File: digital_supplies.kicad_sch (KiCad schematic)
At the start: 74 parts, among them Q1 PMOS, Q2 2PNP, U19 74LVC1G06, U4 3V3REG, U5 LDO-ADJ, U6 LDO-ADJ, U7 LDO-ADJ

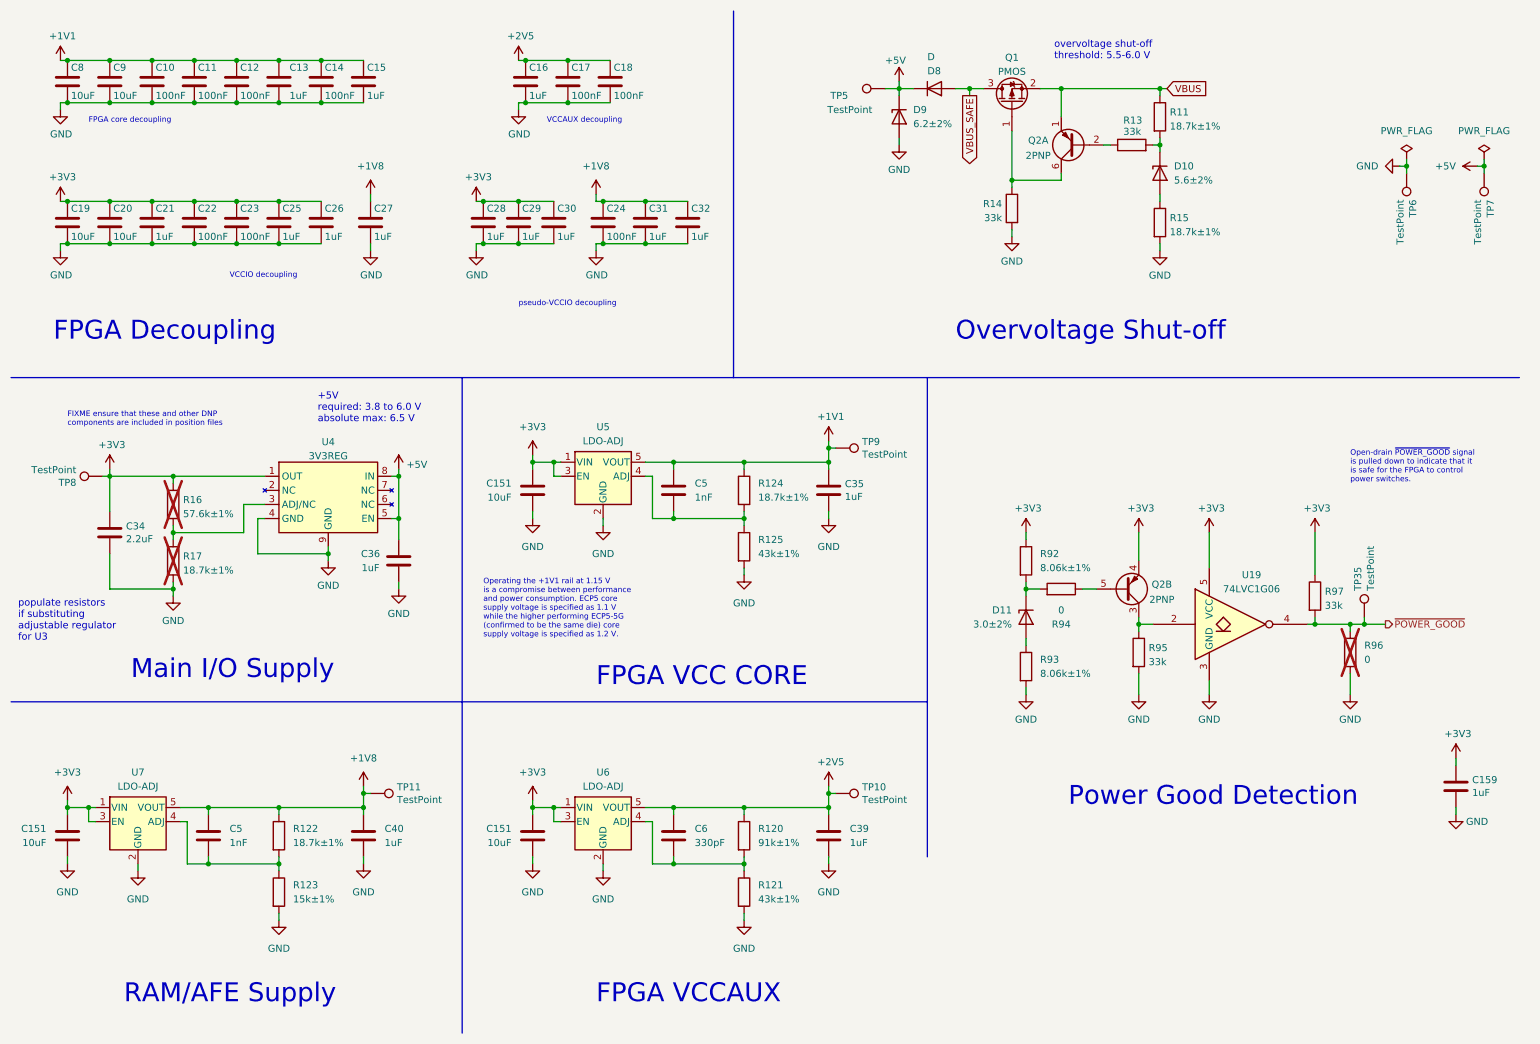
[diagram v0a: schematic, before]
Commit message: add regulator for analog 3.3 V supply
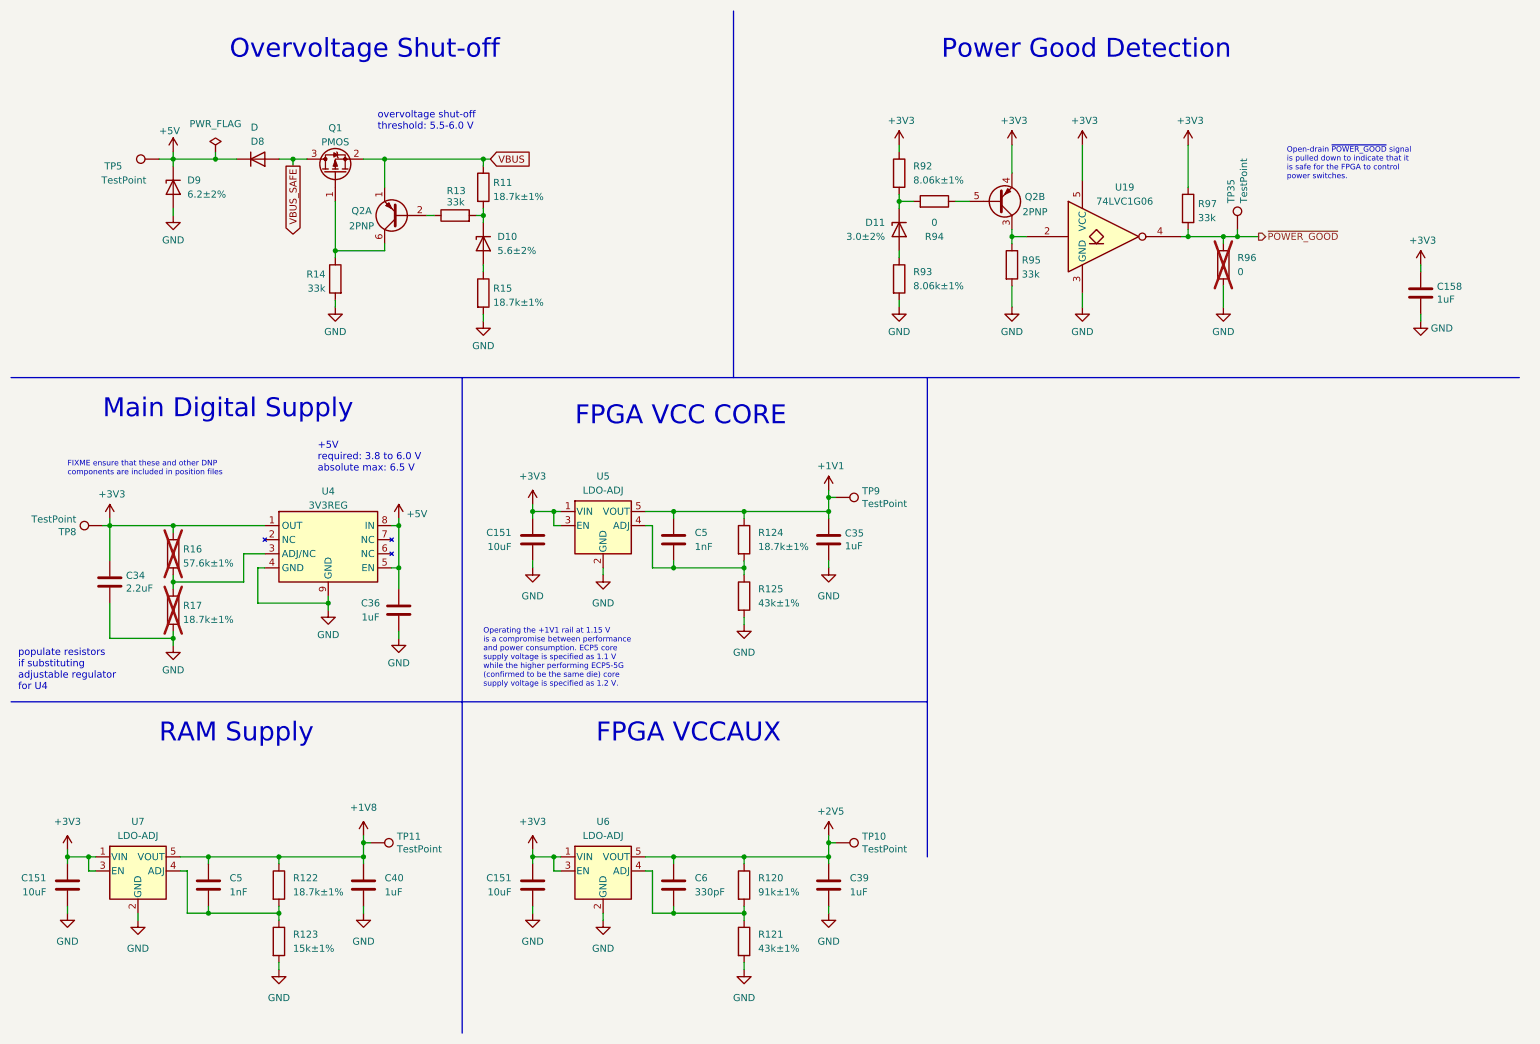
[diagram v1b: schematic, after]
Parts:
- removed C10, C11, C12, C14, C17, C18, C22, C23, C24: 100nF, Capacitor_SMD:C_0402_1005Metric, symbol Device:C
- removed C13, C15, C16, C21, C25, C26, C27, C28, C29, C30, C31, C32: 1uF, Capacitor_SMD:C_0402_1005Metric, symbol Device:C
- removed C19, C20, C8, C9: 10uF, Capacitor_SMD:C_0603_1608Metric, symbol Device:C
- removed TP6, TP7: TestPoint, TestPoint:TestPoint_Pad_D1.0mm, symbol Connector:TestPoint
- renumbered C159 to C158
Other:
- note added: "Main Digital Supply"
- note added: "RAM Supply"
- note added: "populate resistors if substituting adjustable regulator for U4"
- note removed: "FPGA Decoupling"
- note removed: "FPGA core decoupling"
- note removed: "Main I/O Supply"
- note removed: "RAM/AFE Supply"
- note removed: "VCCAUX decoupling"
- note removed: "VCCIO decoupling"
- note removed: "populate resistors if substituting adjustable regulator for U3"
- note removed: "pseudo-VCCIO decoupling"
- moved on the sheet: C151, C158, C34, C35, C36, C39, C40, C5, C6, D10, D11, D8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

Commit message: Add more footprints
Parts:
- D11: footprint cynthion:DFN1006-2 -> mainboard:DFN1006-2
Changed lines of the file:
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@@
       (effects (font (size 1.27 1.27)) (justify left))
     )
-    (property "Footprint" "cynthion:DFN1006-2" (at 172.72 52.07 0)
+    (property "Footprint" "mainboard:DFN1006-2" (at 172.72 52.07 0)
       (effects (font (size 1.27 1.27)) hide)
     )

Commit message: layout wip
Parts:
- C5: footprint Capacitor_SMD:C_0402_1005Metric -> Capacitor_SMD:C_0201_0603Metric; Manufacturer Samsung -> Murata; Part Number CL05B102KB5NNNC -> GRM033R71E102KA01D; Substitution any equivalent -> GRM033R71E102KA01*
- C6: footprint Capacitor_SMD:C_0402_1005Metric -> Capacitor_SMD:C_0201_0603Metric; Manufacturer Samsung -> Murata; Part Number CL05C331JB5NNNC -> GRM0335C1E331JA01D; Substitution any equivalent -> GRM0335C1E331JA01*
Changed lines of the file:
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@@
       (effects (font (size 1.27 1.27)) (justify left))
     )
-    (property "Footprint" "Capacitor_SMD:C_0402_1005Metric" (at 133.0452 111.76 0)
+    (property "Footprint" "Capacitor_SMD:C_0201_0603Metric" (at 133.0452 111.76 0)
       (effects (font (size 1.27 1.27)) hide)
     )
@@
       (effects (font (size 1.27 1.27)) hide)
     )
-    (property "Part Number" "CL05B102KB5NNNC" (at 132.08 107.95 0)
-      (effects (font (size 1.27 1.27)) hide)
-    )
-    (property "Substitution" "any equivalent" (at 132.08 107.95 0)
-      (effects (font (size 1.27 1.27)) hide)
-    )
-    (property "Description" "CAP CER 1000PF 50V X7R 0402" (at 132.08 107.95 0)
-      (effects (font (size 1.27 1.27)) hide)
-    )
-    (property "Manufacturer" "Samsung" (at 132.08 107.95 0)
+    (property "Part Number" "GRM033R71E102KA01D" (at 132.08 107.95 0)
+      (effects (font (size 1.27 1.27)) hide)
+    )
+    (property "Substitution" "GRM033R71E102KA01*" (at 132.08 107.95 0)
+      (effects (font (size 1.27 1.27)) hide)
+    )
+    (property "Description" "CAP CER 1000PF 25V X7R 0201" (at 132.08 107.95 0)
+      (effects (font (size 1.27 1.27)) hide)
+    )
+    (property "Manufacturer" "Murata" (at 132.08 107.95 0)
       (effects (font (size 1.27 1.27)) hide)
     )
@@
       (effects (font (size 1.27 1.27)) (justify left))
     )
-    (property "Footprint" "Capacitor_SMD:C_0402_1005Metric" (at 133.0452 173.99 0)
+    (property "Footprint" "Capacitor_SMD:C_0201_0603Metric" (at 133.0452 173.99 0)
       (effects (font (size 1.27 1.27)) hide)
     )
@@
       (effects (font (size 1.27 1.27)) hide)
     )
-    (property "Part Number" "CL05C331JB5NNNC" (at 132.08 170.18 0)
-      (effects (font (size 1.27 1.27)) hide)
-    )
-    (property "Substitution" "any equivalent" (at 132.08 170.18 0)
-      (effects (font (size 1.27 1.27)) hide)
-    )
-    (property "Description" "CAP CER 330PF 50V C0G/NP0 0402" (at 132.08 170.18 0)
-      (effects (font (size 1.27 1.27)) hide)
-    )
-    (property "Manufacturer" "Samsung" (at 132.08 170.18 0)
+    (property "Part Number" "GRM0335C1E331JA01D" (at 132.08 170.18 0)
+      (effects (font (size 1.27 1.27)) hide)
+    )
+    (property "Substitution" "GRM0335C1E331JA01*" (at 132.08 170.18 0)
+      (effects (font (size 1.27 1.27)) hide)
+    )
+    (property "Description" "CAP CER 330PF 25V C0G/NP0 0201" (at 132.08 170.18 0)
+      (effects (font (size 1.27 1.27)) hide)
+    )
+    (property "Manufacturer" "Murata" (at 132.08 170.18 0)
       (effects (font (size 1.27 1.27)) hide)
     )
@@
       (effects (font (size 1.27 1.27)) (justify left))
     )
-    (property "Footprint" "Capacitor_SMD:C_0402_1005Metric" (at 49.2252 173.99 0)
+    (property "Footprint" "Capacitor_SMD:C_0201_0603Metric" (at 49.2252 173.99 0)
       (effects (font (size 1.27 1.27)) hide)
     )
@@
       (effects (font (size 1.27 1.27)) hide)
     )
-    (property "Part Number" "CL05B102KB5NNNC" (at 48.26 170.18 0)
-      (effects (font (size 1.27 1.27)) hide)
-    )
-    (property "Substitution" "any equivalent" (at 48.26 170.18 0)
-      (effects (font (size 1.27 1.27)) hide)
-    )
-    (property "Description" "CAP CER 1000PF 50V X7R 0402" (at 48.26 170.18 0)
-      (effects (font (size 1.27 1.27)) hide)
-    )
-    (property "Manufacturer" "Samsung" (at 48.26 170.18 0)
-      (effects (font (size 1.27 1.27)) hide)
-    )
+    (property "Part Number" "GRM033R71E102KA01D" (at 48.26 170.18 0)
+      (effects (font (size 1.27 1.27)) hide)
+    )
+    (property "Substitution" "GRM033R71E102KA01*" (at 48.26 170.18 0)
+      (effects (font (size 1.27 1.27)) hide)
+    )
+    (property "Description" "CAP CER 1000PF 25V X7R 0201" (at 48.26 170.18 0)
+      (effects (font (size 1.27 1.27)) hide)
+    )
+    (property "Manufacturer" "Murata" (at 48.26 170.18 0)
+      (effects (font (size 1.27 1.27)) hide)
+    )

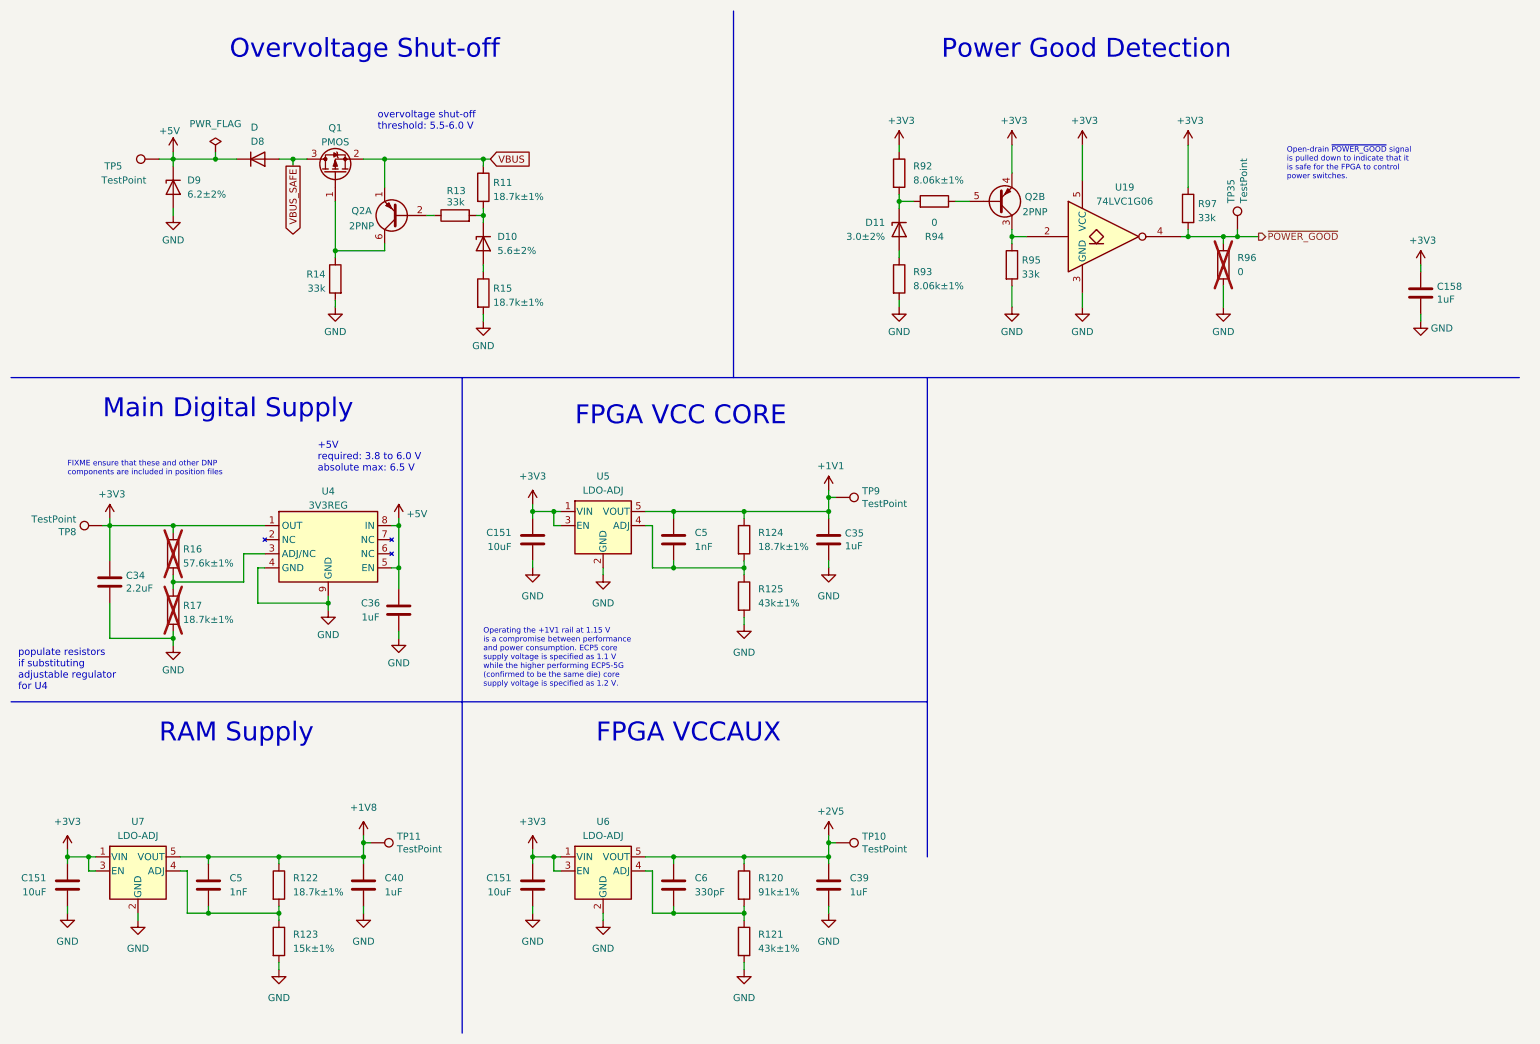
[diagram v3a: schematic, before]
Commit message: complete initial layout
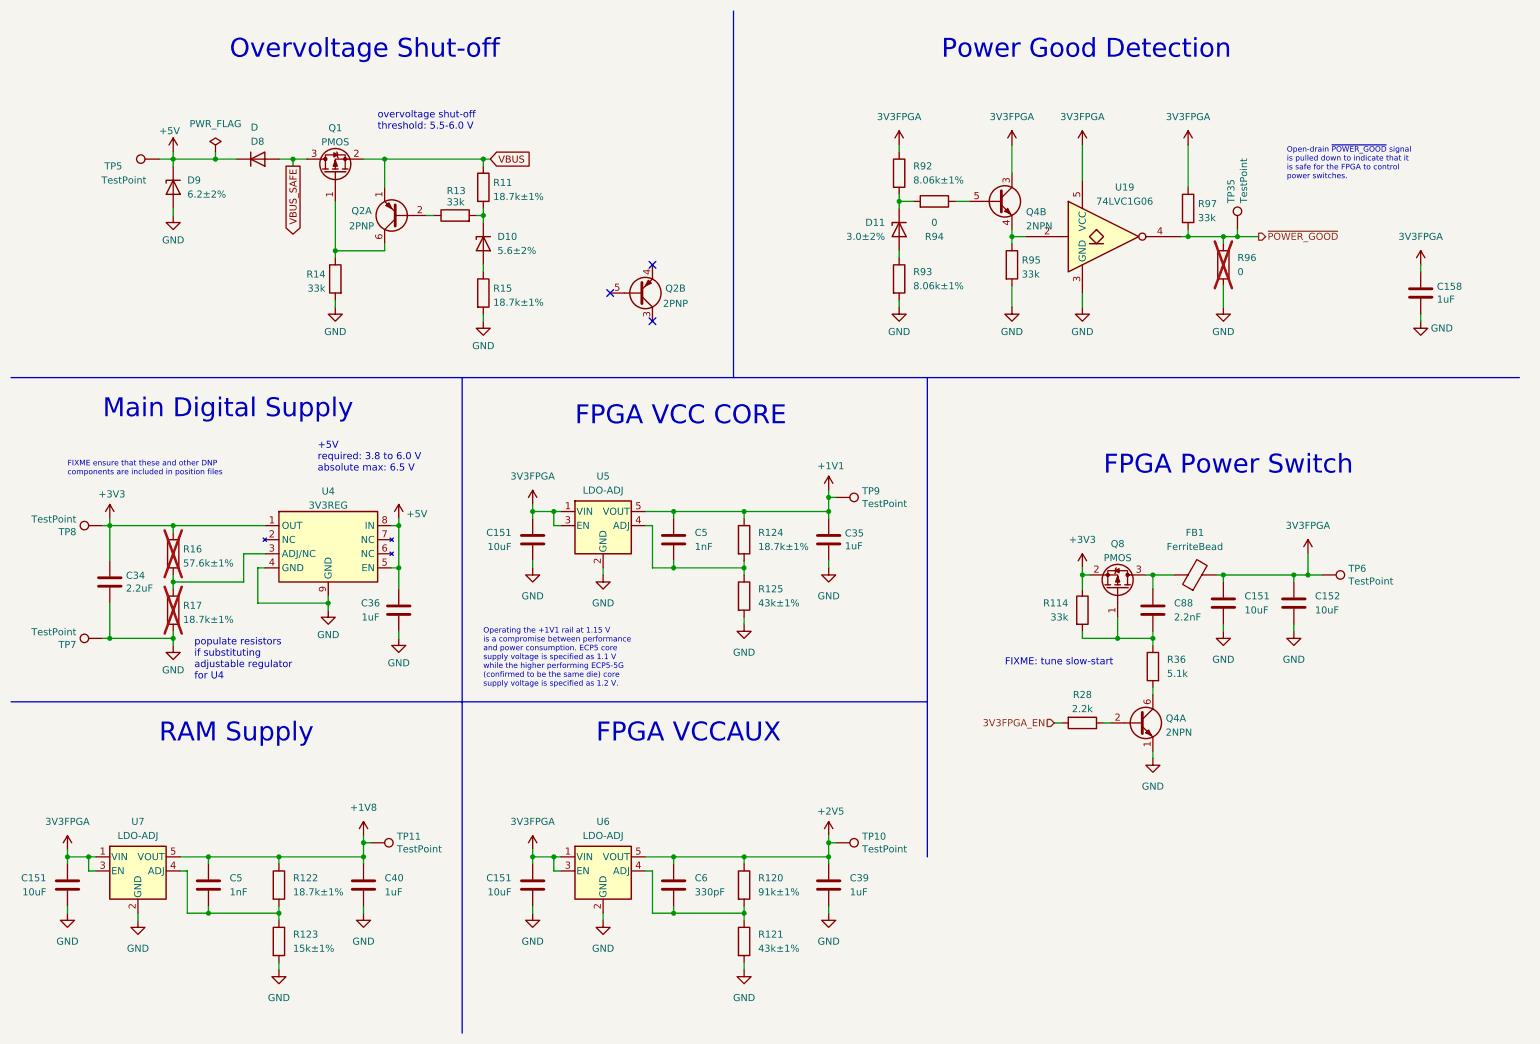
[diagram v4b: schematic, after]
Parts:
- added C151, C152: 10uF, Capacitor_SMD:C_0603_1608Metric, symbol Device:C
- added C88: 2.2nF, Capacitor_SMD:C_0201_0603Metric, symbol Device:C
- added FB1: FerriteBead, Inductor_SMD:L_0603_1608Metric, symbol Device:FerriteBead
- added Q4: 2NPN, Package_TO_SOT_SMD:SOT-363_SC-70-6, symbol Transistor_BJT:BC847BS
- added Q8: PMOS, Package_TO_SOT_SMD:SOT-23-3, symbol Device:Q_PMOS_GSD
- added R114: 33k, Resistor_SMD:R_0402_1005Metric, symbol Device:R
- added R28: 2.2k, Resistor_SMD:R_0402_1005Metric, symbol Device:R
- added R36: 5.1k, Resistor_SMD:R_0402_1005Metric, symbol Device:R
- added TP6, TP7: TestPoint, TestPoint:TestPoint_Pad_D1.0mm, symbol Connector:TestPoint
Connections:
- net +3V3: now also Q8.2 (S), R114.1; no longer C151.1, C151.1, C151.2, C158.1, Q2.4 (E2), R92.1, R97.1, U19.5 (VCC), U5.1 (VIN), U5.3 (EN), U6.1 (VIN), U6.3 (EN), U7.1 (VIN), U7.3 (EN)
- net GND: now also C151.2, C152.2, Q4.1 (E1), TP7.1
- net at R95.1, U19.2: now also Q4.4 (E2); no longer Q2.3 (C2)
- net at Q2.5 (B2): no longer R94.1
- new net: C88.1, Q8.1 (G), R114.2, R36.1
- new net: C88.2, FB1.1, Q8.3 (D)
- new net: Q4.2 (B1), R28.1
- new net: Q4.6 (C1), R36.2
- new net: Q4.5 (B2), R94.1
- new net 3V3FPGA: C151.1, C151.1, C151.1, C151.2, C152.1, C158.1, FB1.2, Q4.3 (C2), R92.1, R97.1, TP6.1, U19.5 (VCC), U5.1 (VIN), U5.3 (EN), U6.1 (VIN), U6.3 (EN), U7.1 (VIN), U7.3 (EN)
- new net 3V3FPGA_EN: R28.2
- no-connect marks 0 -> 3
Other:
- note added: "FIXME: tune slow-start"
- note added: "FPGA Power Switch"
- moved on the sheet: Q2B
